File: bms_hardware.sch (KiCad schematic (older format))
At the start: 0 parts

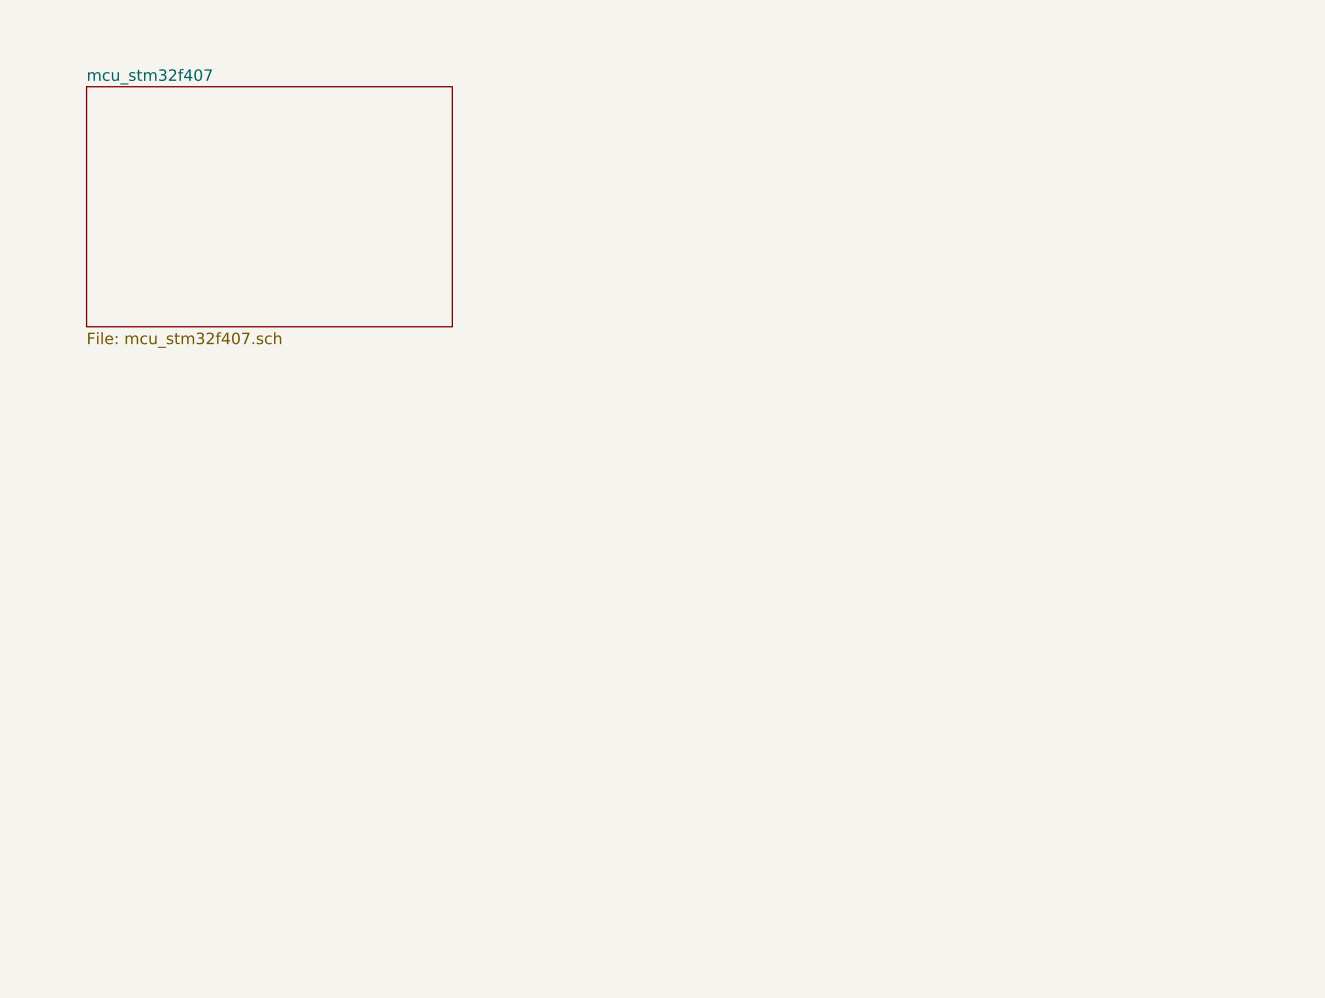
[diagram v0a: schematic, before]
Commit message: mmoya/bq76pl536a Adds bq76p536a
TODO: Calculate resistance divider for temp sensors
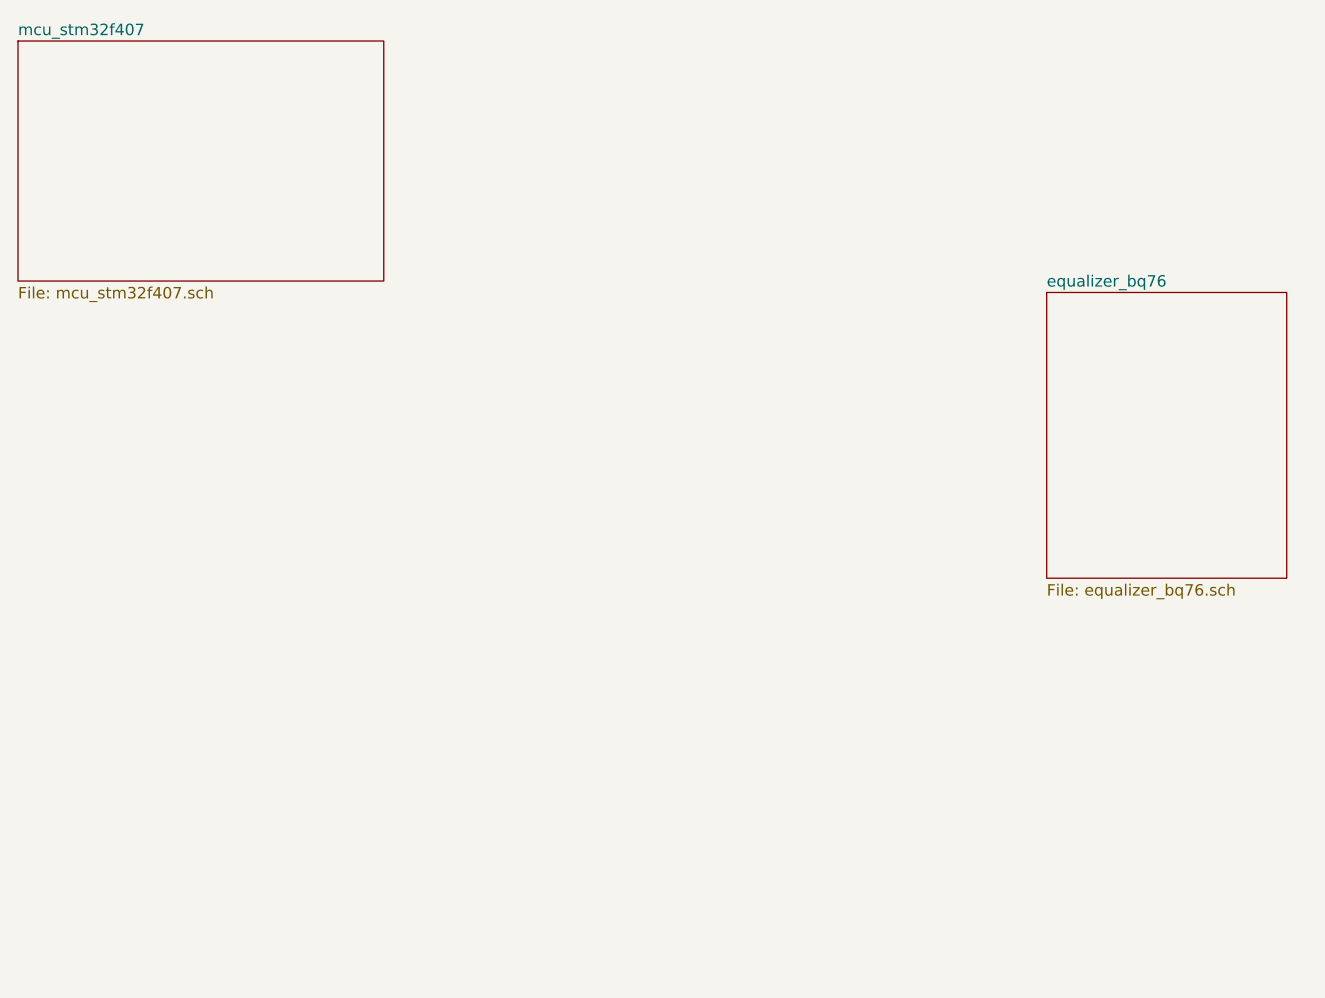
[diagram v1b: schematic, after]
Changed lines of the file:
@@
 $Descr A4 11693 8268
 encoding utf-8
-Sheet 1 2
+Sheet 1 4
 Title ""
 Date ""
@@
 $EndDescr
 $Sheet
-S 3200 1750 1600 1050
+S 2900 1550 1600 1050
 U 5FE4EB49
 F0 "mcu_stm32f407" 50
 F1 "mcu_stm32f407.sch" 50
 $EndSheet
+$Sheet
+S 7400 2650 1050 1250
+U 5FE7678E
+F0 "equalizer_bq76" 50
+F1 "equalizer_bq76.sch" 50
+$EndSheet
 $EndSCHEMATC

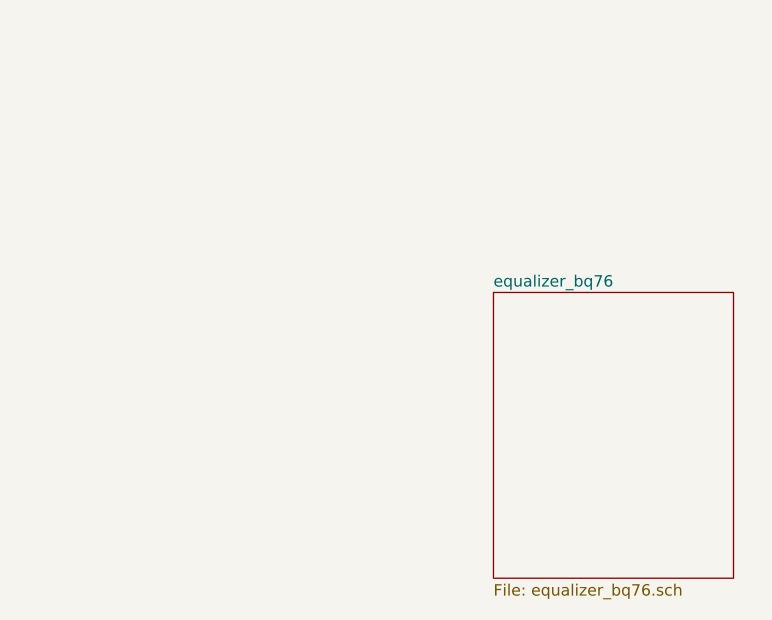
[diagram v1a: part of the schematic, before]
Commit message: mmoya/bq76pl536a Adds current sensor and IO for hierarchical sheet
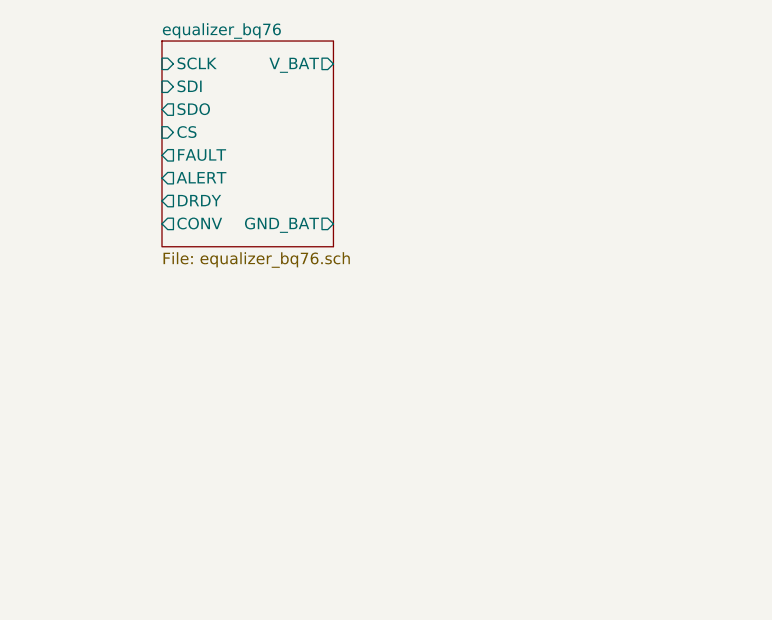
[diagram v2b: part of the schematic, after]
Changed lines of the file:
@@
 $EndSheet
 $Sheet
-S 7400 2650 1050 1250
+S 5950 1550 750  900
 U 5FE7678E
 F0 "equalizer_bq76" 50
 F1 "equalizer_bq76.sch" 50
+F2 "SCLK" I L 5950 1650 50
+F3 "SDI" I L 5950 1750 50
+F4 "SDO" O L 5950 1850 50
+F5 "CS" I L 5950 1950 50
+F6 "FAULT" O L 5950 2050 50
+F7 "ALERT" O L 5950 2150 50
+F8 "DRDY" O L 5950 2250 50
+F9 "CONV" O L 5950 2350 50
+F10 "GND_BAT" O R 6700 2350 50
+F11 "V_BAT" O R 6700 1650 50
 $EndSheet
 $EndSCHEMATC

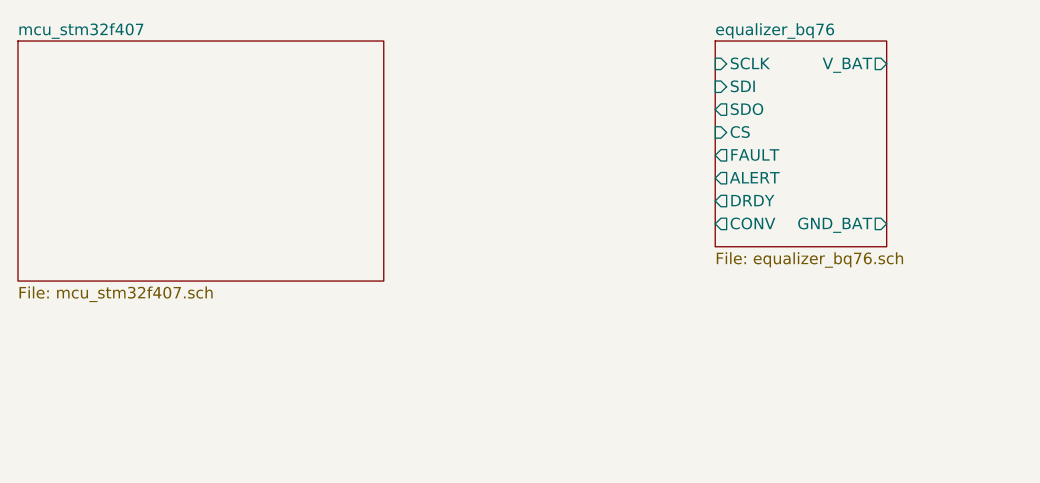
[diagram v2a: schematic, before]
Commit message: Adds missing footprints for conns
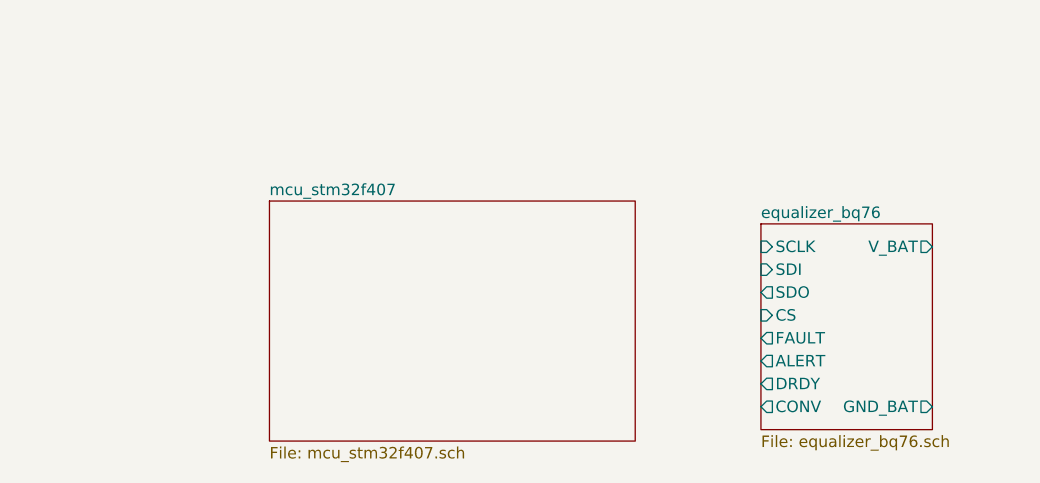
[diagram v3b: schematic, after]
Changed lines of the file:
@@
 $EndDescr
 $Sheet
-S 2900 1550 1600 1050
+S 4000 2250 1600 1050
 U 5FE4EB49
 F0 "mcu_stm32f407" 50
@@
 $EndSheet
 $Sheet
-S 5950 1550 750  900
+S 6150 2350 750  900
 U 5FE7678E
 F0 "equalizer_bq76" 50
 F1 "equalizer_bq76.sch" 50
-F2 "SCLK" I L 5950 1650 50
-F3 "SDI" I L 5950 1750 50
-F4 "SDO" O L 5950 1850 50
-F5 "CS" I L 5950 1950 50
-F6 "FAULT" O L 5950 2050 50
-F7 "ALERT" O L 5950 2150 50
-F8 "DRDY" O L 5950 2250 50
-F9 "CONV" O L 5950 2350 50
-F10 "GND_BAT" O R 6700 2350 50
-F11 "V_BAT" O R 6700 1650 50
+F2 "SCLK" I L 6150 2450 50
+F3 "SDI" I L 6150 2550 50
+F4 "SDO" O L 6150 2650 50
+F5 "CS" I L 6150 2750 50
+F6 "FAULT" O L 6150 2850 50
+F7 "ALERT" O L 6150 2950 50
+F8 "DRDY" O L 6150 3050 50
+F9 "CONV" O L 6150 3150 50
+F10 "GND_BAT" O R 6900 3150 50
+F11 "V_BAT" O R 6900 2450 50
 $EndSheet
 $EndSCHEMATC

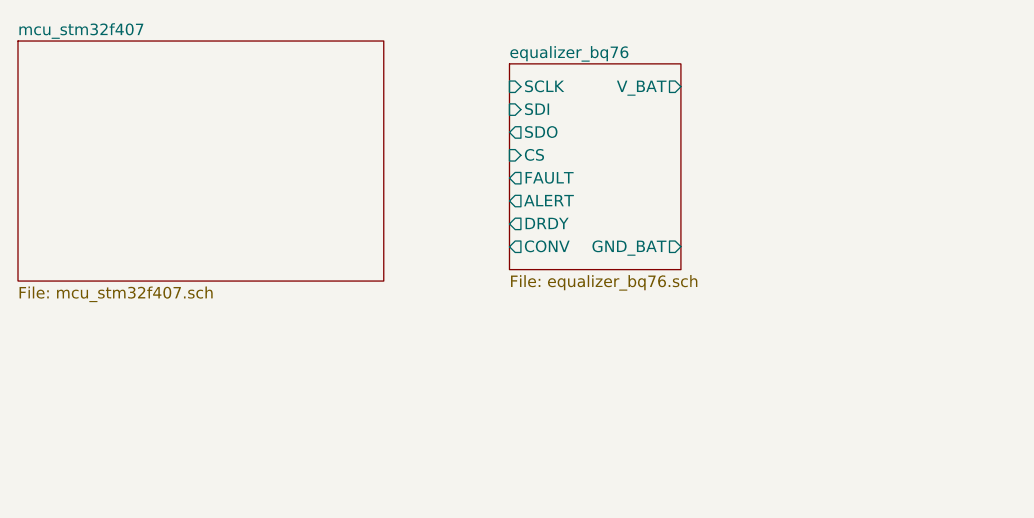
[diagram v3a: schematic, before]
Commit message: mmoya/ina226 Adds ina226 current sensor
- Expects a max current of 20A
- Adds pcb footprint
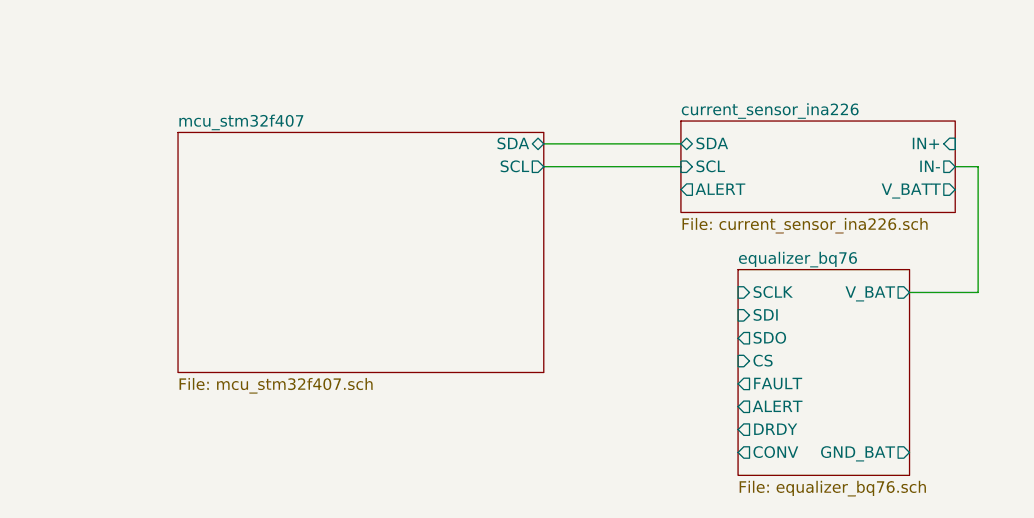
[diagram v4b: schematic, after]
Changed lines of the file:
@@
 $Descr A4 11693 8268
 encoding utf-8
-Sheet 1 4
+Sheet 1 5
 Title ""
 Date ""
@@
 $EndDescr
 $Sheet
-S 4000 2250 1600 1050
+S 4700 2650 1600 1050
 U 5FE4EB49
 F0 "mcu_stm32f407" 50
 F1 "mcu_stm32f407.sch" 50
+F2 "SDA" B R 6300 2700 50
+F3 "SCL" O R 6300 2800 50
 $EndSheet
 $Sheet
-S 6150 2350 750  900
+S 7150 3250 750  900
 U 5FE7678E
 F0 "equalizer_bq76" 50
 F1 "equalizer_bq76.sch" 50
-F2 "SCLK" I L 6150 2450 50
-F3 "SDI" I L 6150 2550 50
-F4 "SDO" O L 6150 2650 50
-F5 "CS" I L 6150 2750 50
-F6 "FAULT" O L 6150 2850 50
-F7 "ALERT" O L 6150 2950 50
-F8 "DRDY" O L 6150 3050 50
-F9 "CONV" O L 6150 3150 50
-F10 "GND_BAT" O R 6900 3150 50
-F11 "V_BAT" O R 6900 2450 50
+F2 "SCLK" I L 7150 3350 50
+F3 "SDI" I L 7150 3450 50
+F4 "SDO" O L 7150 3550 50
+F5 "CS" I L 7150 3650 50
+F6 "FAULT" O L 7150 3750 50
+F7 "ALERT" O L 7150 3850 50
+F8 "DRDY" O L 7150 3950 50
+F9 "CONV" O L 7150 4050 50
+F10 "GND_BAT" O R 7900 4050 50
+F11 "V_BAT" O R 7900 3350 50
 $EndSheet
+$Sheet
+S 6900 2600 1200 400
+U 5FE91E2B
+F0 "current_sensor_ina226" 50
+F1 "current_sensor_ina226.sch" 50
+F2 "SDA" B L 6900 2700 50
+F3 "SCL" I L 6900 2800 50
+F4 "ALERT" O L 6900 2900 50
+F5 "IN+" I R 8100 2700 50
+F6 "IN-" O R 8100 2800 50
+F7 "V_BATT" O R 8100 2900 50
+$EndSheet
+Wire Wire Line
+	6300 2700 6900 2700
+Wire Wire Line
+	7900 3350 8200 3350
+Wire Wire Line
+	8200 3350 8200 2800
+Wire Wire Line
+	8200 2800 8100 2800
+Wire Wire Line
+	6300 2800 6900 2800
 $EndSCHEMATC

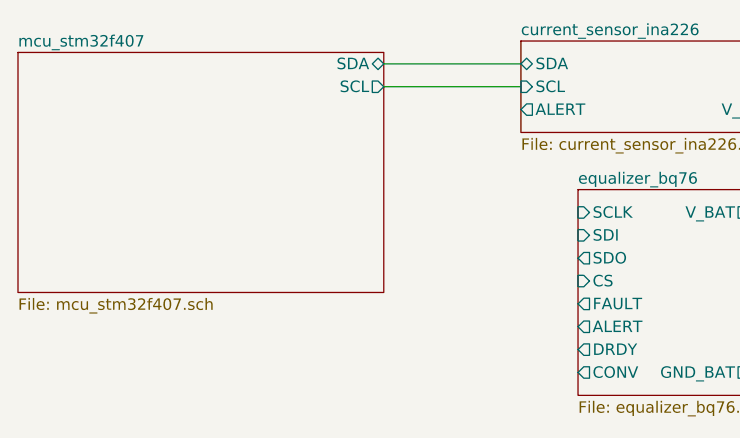
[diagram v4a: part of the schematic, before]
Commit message: Adds SPI port to STM32F407VGxx
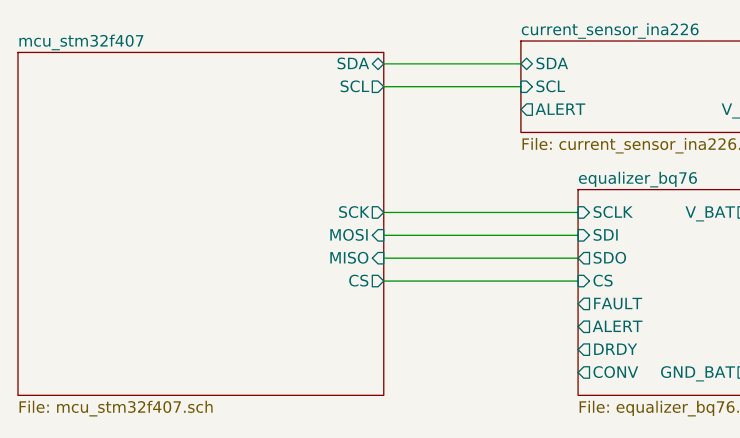
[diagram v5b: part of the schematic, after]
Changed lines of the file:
@@
 $EndDescr
-$Sheet
-S 4700 2650 1600 1050
-U 5FE4EB49
-F0 "mcu_stm32f407" 50
-F1 "mcu_stm32f407.sch" 50
-F2 "SDA" B R 6300 2700 50
-F3 "SCL" O R 6300 2800 50
-$EndSheet
 $Sheet
 S 7150 3250 750  900
@@
 Wire Wire Line
 	6300 2800 6900 2800
+Wire Wire Line
+	6300 3450 7150 3450
+Wire Wire Line
+	6300 3350 7150 3350
+Wire Wire Line
+	6300 3550 7150 3550
+Wire Wire Line
+	6300 3650 7150 3650
+$Sheet
+S 4700 2650 1600 1500
+U 5FE4EB49
+F0 "mcu_stm32f407" 50
+F1 "mcu_stm32f407.sch" 50
+F2 "SDA" B R 6300 2700 50
+F3 "SCL" O R 6300 2800 50
+F4 "SCK" O R 6300 3350 50
+F5 "MISO" I R 6300 3550 50
+F6 "MOSI" I R 6300 3450 50
+F7 "CS" O R 6300 3650 50
+$EndSheet
 $EndSCHEMATC

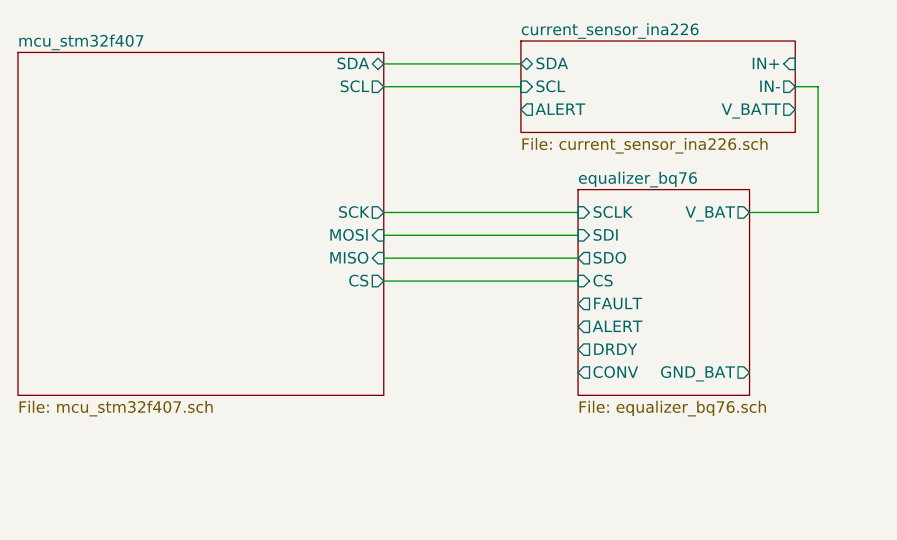
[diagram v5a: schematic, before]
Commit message: Changes overlapping names of pins between bq76 and ina226
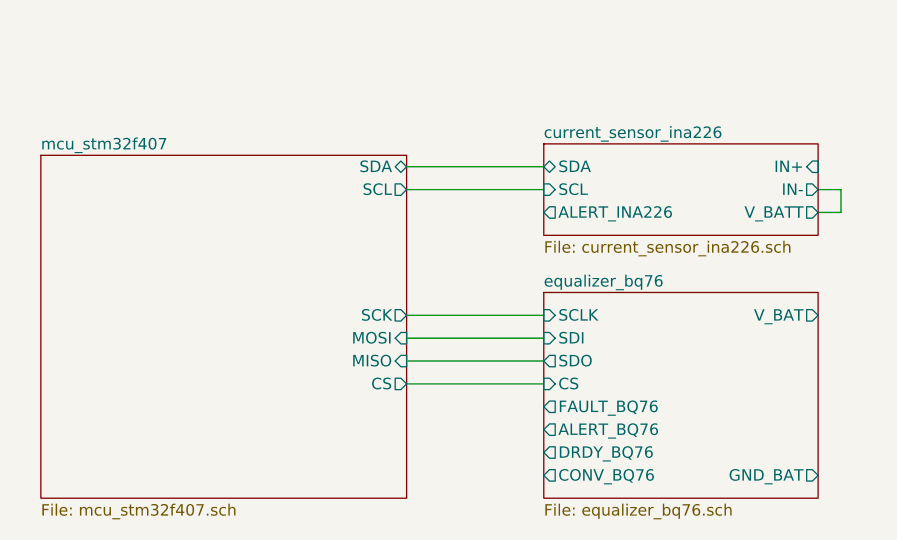
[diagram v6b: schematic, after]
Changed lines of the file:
@@
 $EndDescr
 $Sheet
-S 7150 3250 750  900
+S 7000 3050 1200 400
+U 5FE91E2B
+F0 "current_sensor_ina226" 50
+F1 "current_sensor_ina226.sch" 50
+F2 "SDA" B L 7000 3150 50
+F3 "SCL" I L 7000 3250 50
+F4 "IN+" I R 8200 3150 50
+F5 "IN-" O R 8200 3250 50
+F6 "V_BATT" O R 8200 3350 50
+F7 "ALERT_INA226" O L 7000 3350 50
+$EndSheet
+Wire Wire Line
+	6400 3150 7000 3150
+Wire Wire Line
+	8300 3250 8200 3250
+Wire Wire Line
+	6400 3250 7000 3250
+$Sheet
+S 4800 3100 1600 1500
+U 5FE4EB49
+F0 "mcu_stm32f407" 50
+F1 "mcu_stm32f407.sch" 50
+F2 "SDA" B R 6400 3150 50
+F3 "SCL" O R 6400 3250 50
+F4 "SCK" O R 6400 3800 50
+F5 "MISO" I R 6400 4000 50
+F6 "MOSI" I R 6400 3900 50
+F7 "CS" O R 6400 4100 50
+$EndSheet
+Wire Wire Line
+	8200 3350 8300 3350
+Wire Wire Line
+	8300 3350 8300 3250
+$Sheet
+S 7000 3700 1200 900
 U 5FE7678E
 F0 "equalizer_bq76" 50
 F1 "equalizer_bq76.sch" 50
-F2 "SCLK" I L 7150 3350 50
-F3 "SDI" I L 7150 3450 50
-F4 "SDO" O L 7150 3550 50
-F5 "CS" I L 7150 3650 50
-F6 "FAULT" O L 7150 3750 50
-F7 "ALERT" O L 7150 3850 50
-F8 "DRDY" O L 7150 3950 50
-F9 "CONV" O L 7150 4050 50
-F10 "GND_BAT" O R 7900 4050 50
-F11 "V_BAT" O R 7900 3350 50
-$EndSheet
-$Sheet
-S 6900 2600 1200 400
-U 5FE91E2B
-F0 "current_sensor_ina226" 50
-F1 "current_sensor_ina226.sch" 50
-F2 "SDA" B L 6900 2700 50
-F3 "SCL" I L 6900 2800 50
-F4 "ALERT" O L 6900 2900 50
-F5 "IN+" I R 8100 2700 50
-F6 "IN-" O R 8100 2800 50
-F7 "V_BATT" O R 8100 2900 50
+F2 "SCLK" I L 7000 3800 50
+F3 "SDI" I L 7000 3900 50
+F4 "SDO" O L 7000 4000 50
+F5 "CS" I L 7000 4100 50
+F6 "GND_BAT" O R 8200 4500 50
+F7 "V_BAT" O R 8200 3800 50
+F8 "FAULT_BQ76" O L 7000 4200 50
+F9 "ALERT_BQ76" O L 7000 4300 50
+F10 "DRDY_BQ76" O L 7000 4400 50
+F11 "CONV_BQ76" O L 7000 4500 50
 $EndSheet
 Wire Wire Line
-	6300 2700 6900 2700
+	6400 3800 7000 3800
 Wire Wire Line
-	7900 3350 8200 3350
+	6400 3900 7000 3900
 Wire Wire Line
-	8200 3350 8200 2800
+	6400 4000 7000 4000
 Wire Wire Line
-	8200 2800 8100 2800
-Wire Wire Line
-	6300 2800 6900 2800
-Wire Wire Line
-	6300 3450 7150 3450
-Wire Wire Line
-	6300 3350 7150 3350
-Wire Wire Line
-	6300 3550 7150 3550
-Wire Wire Line
-	6300 3650 7150 3650
-$Sheet
-S 4700 2650 1600 1500
-U 5FE4EB49
-F0 "mcu_stm32f407" 50
-F1 "mcu_stm32f407.sch" 50
-F2 "SDA" B R 6300 2700 50
-F3 "SCL" O R 6300 2800 50
-F4 "SCK" O R 6300 3350 50
-F5 "MISO" I R 6300 3550 50
-F6 "MOSI" I R 6300 3450 50
-F7 "CS" O R 6300 3650 50
-$EndSheet
+	6400 4100 7000 4100
 $EndSCHEMATC
